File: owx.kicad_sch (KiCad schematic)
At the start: 6 parts, among them J21 Conn_02x02_Top_Bottom, U12 LTC4311, U13 DS18B20U

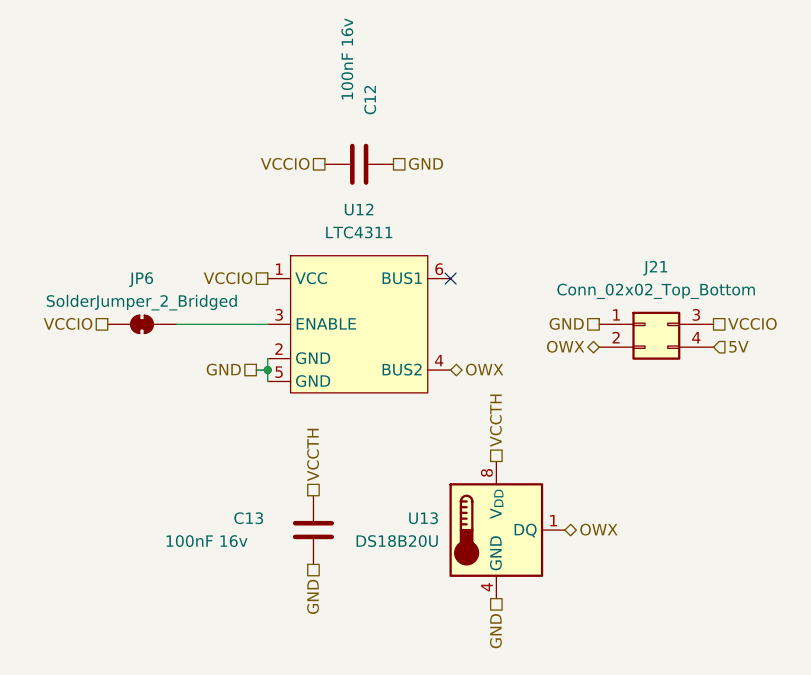
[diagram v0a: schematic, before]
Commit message: i2c, servo, pcb: pca9685 servo, pcb, rs422: leds
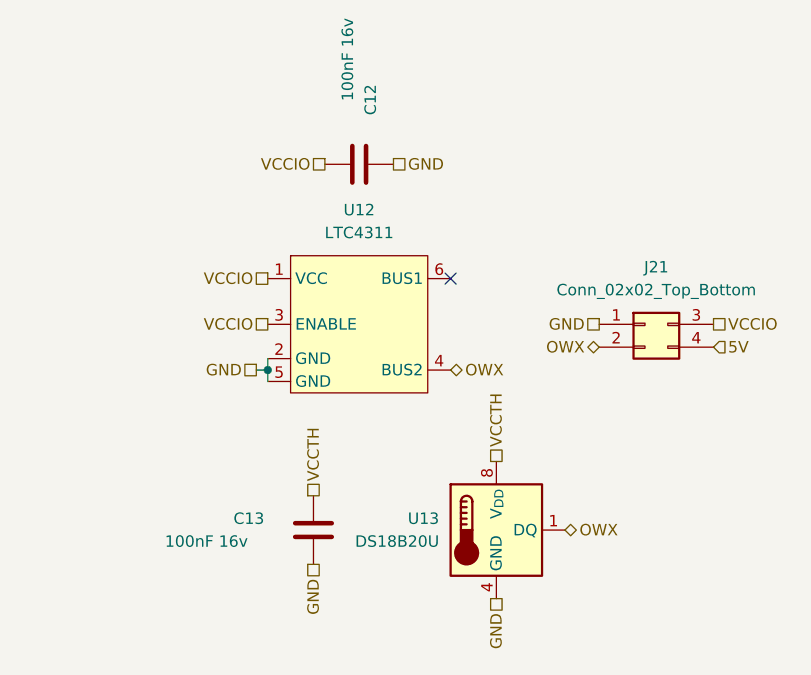
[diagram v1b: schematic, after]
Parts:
- removed JP6: SolderJumper_2_Bridged, Jumper:SolderJumper-2_P1.3mm_Bridged_RoundedPad1.0x1.5mm, symbol Jumper:SolderJumper_2_Bridged
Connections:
- net VCCIO: now also U12.3 (ENABLE)
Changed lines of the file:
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@@
-		)
-	)
-	(wire
-		(pts
-			(xy 115.57 107.95) (xy 125.73 107.95)
-		)
-		(stroke
-			(width 0)
-			(type default)
 		)
 	)
@@
 	(hierarchical_label "VCCIO"
 		(shape passive)
-		(at 107.95 107.95 180)
+		(at 125.73 107.95 180)
 		(effects
 			(font
@@
 					(unit 1)
 				)
-			)
-		)
-	)
-	(symbol
-		(lib_id "Jumper:SolderJumper_2_Bridged")
-		(at 111.76 107.95 0)
-		(unit 1)
-		(exclude_from_sim no)
-		(in_bom no)
-		(on_board yes)
-		(dnp no)
-		(property "Reference" "JP6"
-			(at 111.76 102.87 0)
-			(effects
-				(font
-					(size 1.27 1.27)
-				)
-			)
-		)
-		(property "Value" "SolderJumper_2_Bridged"
-			(at 111.76 105.41 0)
-			(effects
-				(font
-					(size 1.27 1.27)
-				)
-			)
-		)
-		(property "Footprint" "Jumper:SolderJumper-2_P1.3mm_Bridged_RoundedPad1.0x1.5mm"
-			(at 111.76 107.95 0)
-			(effects
-				(font
-					(size 1.27 1.27)
-				)
-				(hide yes)
-			)
-		)
-		(property "Datasheet" "~"
-			(at 111.76 107.95 0)
-			(effects
-				(font
-					(size 1.27 1.27)
-				)
-				(hide yes)
-			)
-		)
-		(property "Description" "Solder Jumper, 2-pole, closed/bridged"
-			(at 111.76 107.95 0)
-			(effects
-				(font
-					(size 1.27 1.27)
-				)
-				(hide yes)
-			)
-		)
-		(pin "2"
-		)
-		(pin "1"
-		)
-		(instances
-			(project "P2 Kevinbot Board"
-				(path "/362ca48c-0b77-4943-b8b3-fc15ab97f30d/5453e275-4798-490a-963f-0bb3e1119943"
-					(reference "JP6")
-					(unit 1)
-				)

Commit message: Part numbers
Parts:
- J21: Part Number (none) -> 1053101104
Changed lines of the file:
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@@
+			)
+		)
+		(property "Part Number" "1053101104"
+			(at 167.64 107.95 0)
+			(effects
+				(font
+					(size 1.27 1.27)
+				)
+				(hide yes)
 			)
 		)
